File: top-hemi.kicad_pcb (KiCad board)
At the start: 2 copper layers, 46 x 39 mm, 38 parts, among them J1 USB_B_Mini, J2 TC2030_NL, J3 FFC-0.5MM-6POS, J4 Conn_01x02, J5 Conn_01x02, J6 FFC-0.5MM-6POS, J7 Conn_01x02, J8 Conn_01x02, U1 PMIC-LDO-XC6204B332MR_SOT23-5_, U2 LP2985-5.0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

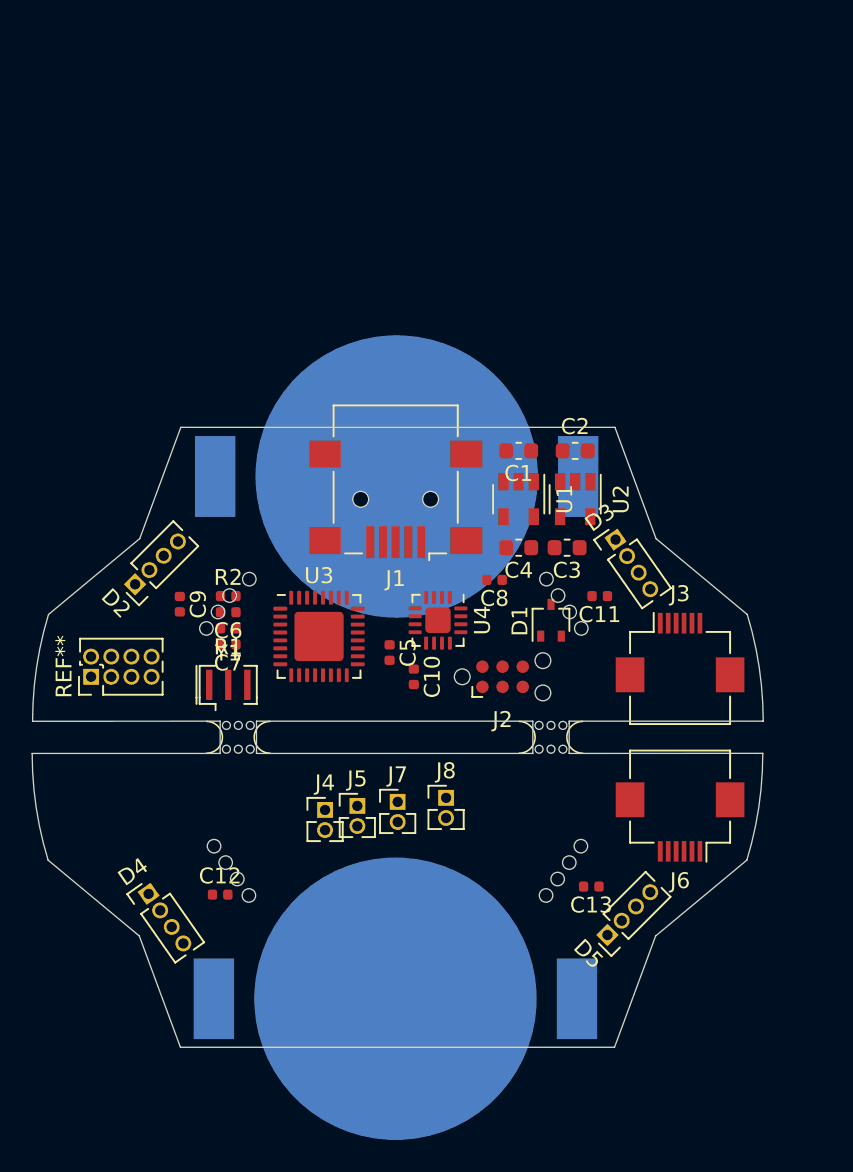
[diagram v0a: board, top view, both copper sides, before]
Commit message: Move BNC connectors to correct hemispheres
Positions within the hemisphere don’t matter.
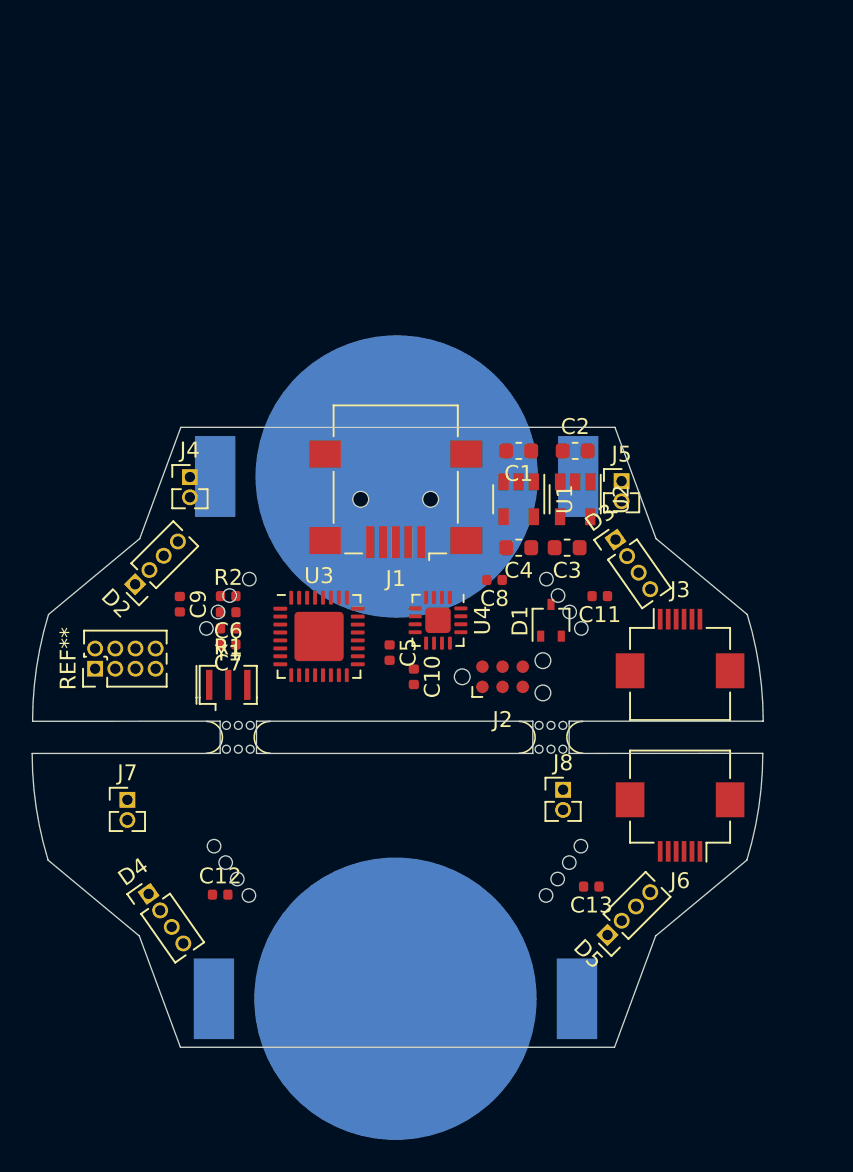
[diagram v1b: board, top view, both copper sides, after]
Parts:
- J4: value Conn_01x02 -> Port_1
- J5: value Conn_01x02 -> Port_2
- J7: value Conn_01x02 -> Port_3
- J8: value Conn_01x02 -> Port_4
- moved J5 26.4 mm to (147.2, 72.5)
- moved J4 22.6 mm to (120.0, 72.3)
- moved J7 17.0 mm to (116.1, 92.6)
- moved J8 7.38 mm to (143.5, 91.9)
- moved REF** 0.57 mm to (114.0, 84.3)
- moved J3 0.25 mm to (150.9, 83.1)
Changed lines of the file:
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@@
   (general
     (thickness 1.6)
-    (drawings 116)
+    (drawings 117)
     (tracks 0)
     (zones 0)
@@
     (0 F.Cu signal)
     (31 B.Cu signal hide)
-    (32 B.Adhes user)
-    (33 F.Adhes user)
-    (34 B.Paste user)
+    (32 B.Adhes user hide)
+    (33 F.Adhes user hide)
+    (34 B.Paste user hide)
     (35 F.Paste user)
-    (36 B.SilkS user)
-    (37 F.SilkS user)
+    (36 B.SilkS user hide)
+    (37 F.SilkS user hide)
     (38 B.Mask user hide)
-    (39 F.Mask user hide)
-    (40 Dwgs.User user hide)
+    (39 F.Mask user)
+    (40 Dwgs.User user)
     (41 Cmts.User user hide)
     (42 Eco1.User user hide)
     (43 Eco2.User user hide)
     (44 Edge.Cuts user)
-    (45 Margin user)
+    (45 Margin user hide)
     (46 B.CrtYd user hide)
-    (47 F.CrtYd user hide)
+    (47 F.CrtYd user)
     (48 B.Fab user hide)
-    (49 F.Fab user hide)
+    (49 F.Fab user)
   )
   (setup
@@
   )
   (module Connector_PinHeader_1.27mm:PinHeader_2x04_P1.27mm_Vertical (layer F.Cu)
-    (at 113.792 84.836 90)
+    (at 114.046 84.328 90)
     (descr "Through hole straight pin header, 2x04, 1.27mm pitch, double rows")
     (tags "Through hole pin header THT 2x04 1.27mm double row")
@@
       (effects (font (size 1 1) (thickness 0.15)))
     )
-    (fp_text user %R (at 0.635 1.905 180) (layer F.Fab)
+    (fp_text user %R (at -2.413 0.762 180) (layer F.Fab)
       (effects (font (size 1 1) (thickness 0.15)))
     )
@@
   )
   (module Connector_FFC-FPC:Hirose_FH12-6S-0.5SH_1x06-1MP_P0.50mm_Horizontal (layer F.Cu)
-    (at 150.876 83.312)
+    (at 150.876 83.058)
     (descr "Molex FH12, FFC/FPC connector, FH12-6S-0.5SH, 6 Pins per row (https://www.hirose.com/product/en/products/FH12/FH12-24S-0.5SH(55)/), generated with kicad-footprint-generator")
     (tags "connector Hirose  top entry")
@@
     (fp_line (start 1.55 4.95) (end 1.55 -1.15) (layer F.CrtYd) (width 0.05))
     (fp_line (start 1.55 -1.15) (end -1.55 -1.15) (layer F.CrtYd) (width 0.05))
-    (fp_text user %R (at 0 1.905 225) (layer F.Fab)
+    (fp_text user %R (at 0.987828 5.862694 225) (layer F.Fab)
       (effects (font (size 1 1) (thickness 0.15)))
     )
@@
   )
   (module Connector_PinHeader_1.27mm:PinHeader_1x02_P1.27mm_Vertical (layer F.Cu)
-    (at 128.524 93.218)
+    (at 120.015 72.263)
     (descr "Through hole straight pin header, 1x02, 1.27mm pitch, single row")
     (tags "Through hole pin header THT 1x02 1.27mm single row")
@@
       (effects (font (size 1 1) (thickness 0.15)))
     )
-    (fp_text value Conn_01x02 (at 0 2.965) (layer F.Fab)
+    (fp_text value Port_1 (at 0 2.965) (layer F.Fab)
       (effects (font (size 1 1) (thickness 0.15)))
     )
@@
   )
   (module Connector_PinHeader_1.27mm:PinHeader_1x02_P1.27mm_Vertical (layer F.Cu)
-    (at 130.556 92.964)
+    (at 147.193 72.517)
     (descr "Through hole straight pin header, 1x02, 1.27mm pitch, single row")
     (tags "Through hole pin header THT 1x02 1.27mm single row")
@@
       (effects (font (size 1 1) (thickness 0.15)))
     )
-    (fp_text value Conn_01x02 (at 0 2.965) (layer F.Fab)
+    (fp_text value Port_2 (at 0 2.965) (layer F.Fab)
       (effects (font (size 1 1) (thickness 0.15)))
     )
@@
   )
   (module Connector_PinHeader_1.27mm:PinHeader_1x02_P1.27mm_Vertical (layer F.Cu)
-    (at 133.096 92.71)
+    (at 116.078 92.583)
     (descr "Through hole straight pin header, 1x02, 1.27mm pitch, single row")
     (tags "Through hole pin header THT 1x02 1.27mm single row")
@@
       (effects (font (size 1 1) (thickness 0.15)))
     )
-    (fp_text value Conn_01x02 (at 0 2.965) (layer F.Fab)
+    (fp_text value Port_3 (at 0 2.965) (layer F.Fab)
       (effects (font (size 1 1) (thickness 0.15)))
     )
@@
   )
   (module Connector_PinHeader_1.27mm:PinHeader_1x02_P1.27mm_Vertical (layer F.Cu)
-    (at 136.144 92.456)
+    (at 143.51 91.948)
     (descr "Through hole straight pin header, 1x02, 1.27mm pitch, single row")
     (tags "Through hole pin header THT 1x02 1.27mm single row")
@@
       (effects (font (size 1 1) (thickness 0.15)))
     )
-    (fp_text value Conn_01x02 (at 0 2.965) (layer F.Fab)
+    (fp_text value Port_4 (at 0 2.965) (layer F.Fab)
       (effects (font (size 1 1) (thickness 0.15)))
     )
@@
       (net 4 "/Bottom hemisphere/BATT-BOT") (die_length 0.20066))
   )
+  (gr_circle (center 152.019 76.708) (end 152.319 76.708) (layer Dwgs.User) (width 0.01))
   (gr_line (start 143.891 87.63) (end 143.891 87.757) (layer Edge.Cuts) (width 0.05))
   (gr_line (start 156.109 87.63) (end 143.891 87.63) (layer Edge.Cuts) (width 0.05))

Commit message: Update contours
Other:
- board size 46 x 39 mm -> 49.7 x 63.9 mm

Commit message: Update panelization
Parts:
- moved mouse-bite-2mm-slot 2.03 mm to (125.1, 88.6)
- moved mouse-bite-2mm-slot 1.64 mm to (141.1, 88.6)
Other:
- board size 49.7 x 63.9 mm -> 46 x 39 mm
- board text removed: "Holder w/ battery (Bottom)"
- board text removed: "LED"
- board text removed: "Micr. USB (Top)"
- board text removed: "Rail / Fixture"

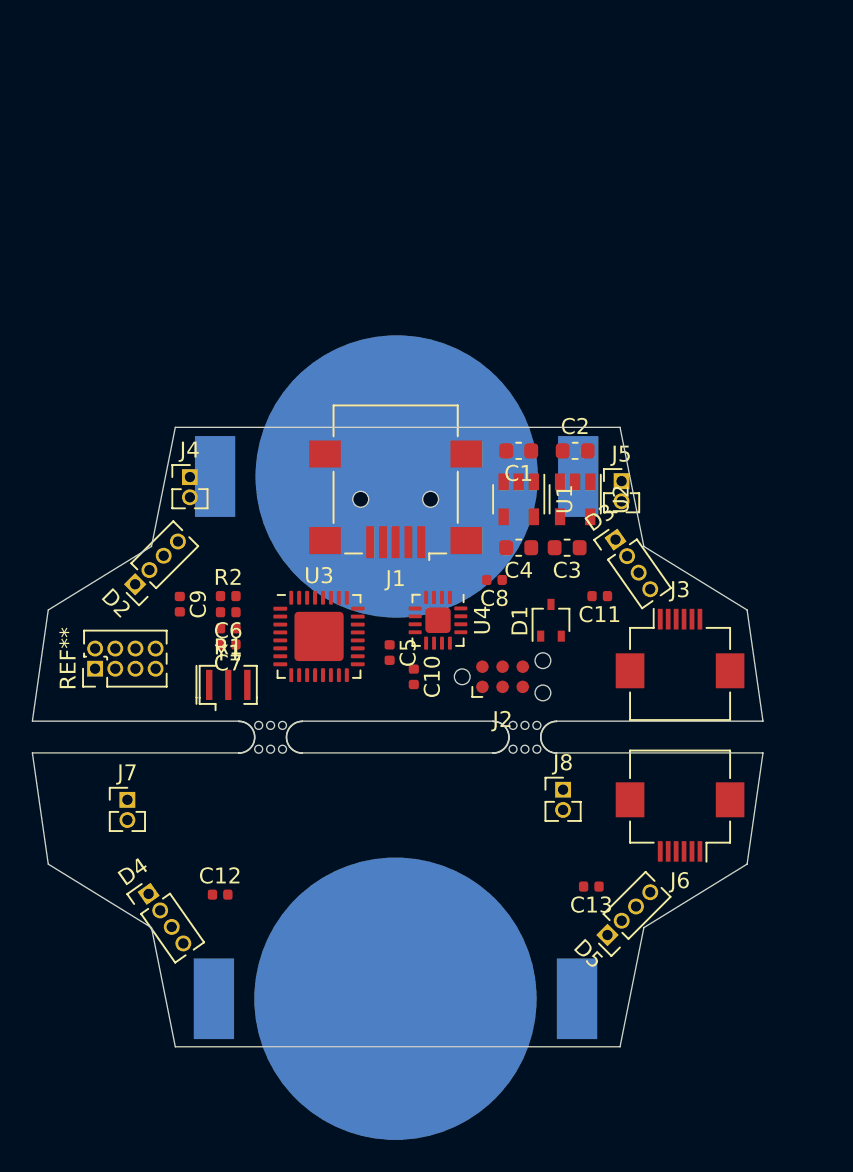
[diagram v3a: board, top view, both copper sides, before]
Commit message: Added initial tracks
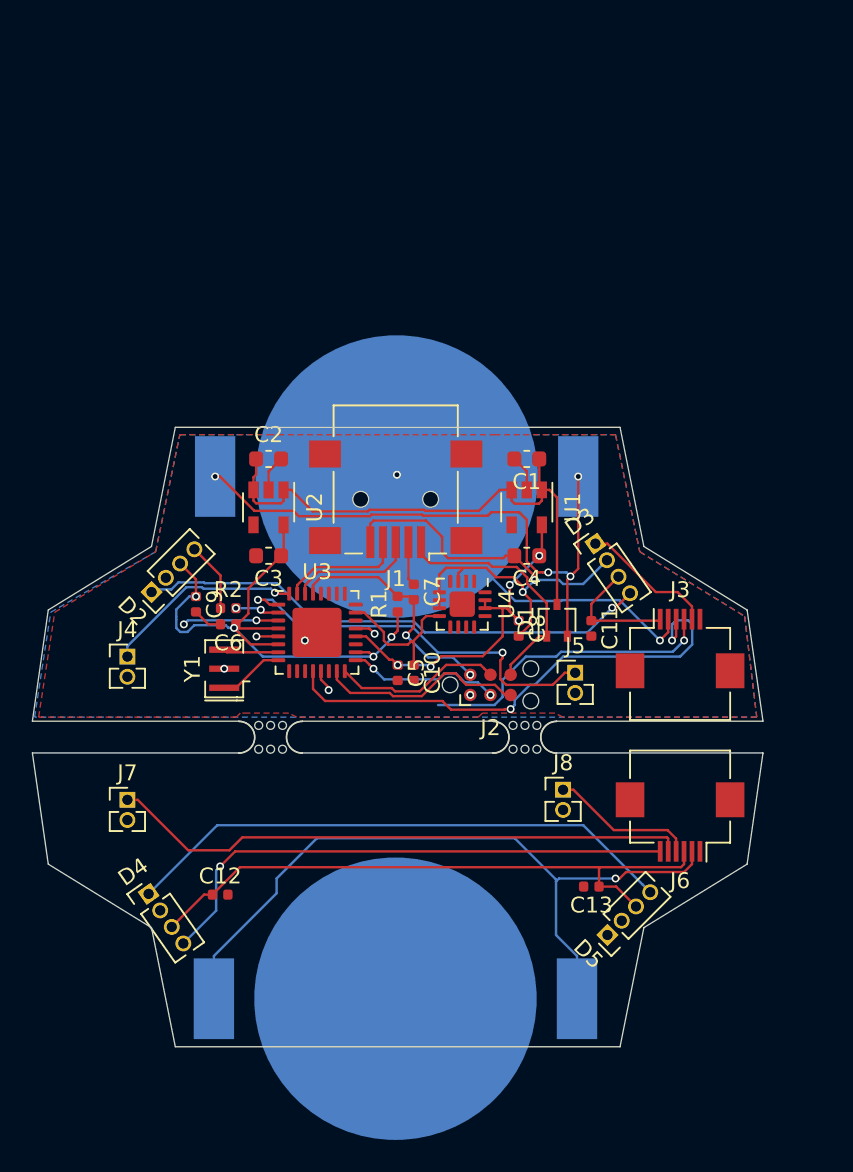
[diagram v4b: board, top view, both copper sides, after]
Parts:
- removed REF**: PinHeader_2x04_P1.27mm_Vertical, Connector_PinHeader_1.27mm:PinHeader_2x04_P1.27mm_Vertical
- moved C2 19.3 mm to (125.0, 71.1)
- moved U2 19.3 mm to (125.0, 74.2)
- moved C3 18.8 mm to (125.0, 77.2)
- moved J5 12.4 mm to (144.3, 84.6)
- moved C7 12.1 mm to (134.1, 79.5), turned to 270 degrees
- moved J4 12.0 mm to (116.1, 83.6)
- moved R1 10.8 mm to (133.1, 80.3), turned to 90 degrees
- moved C8 3.41 mm to (140.7, 81.8), turned to 270 degrees
- moved C11 2.10 mm to (145.3, 81.8), turned to 270 degrees
- moved U4 1.83 mm to (137.2, 80.3)
- moved C5 1.37 mm to (133.1, 84.6)
- moved D3 1.30 mm to (145.5, 76.5)
- moved D2 1.14 mm to (117.6, 79.5)
- moved Y1 1.05 mm to (122.2, 84.3), turned to 90 degrees
- moved C9 1.02 mm to (120.4, 80.3)
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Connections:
- J1 pad 2: /Top Hemisphere/RXI -> /Top Hemisphere/DTR
- J1 pad 3: /Top Hemisphere/DTR -> /Top Hemisphere/RXI
- J1 pad 6: GND -> Net-(J1-Pad6)
- J2 pad 1: /Top Hemisphere/+5V_EXT -> GND
- J2 pad 2: /Top Hemisphere/MOSI -> /Top Hemisphere/~RST
- J2 pad 3: /Top Hemisphere/MISO -> /Top Hemisphere/SCK
- J2 pad 4: /Top Hemisphere/SCK -> /Top Hemisphere/MISO
- J2 pad 5: /Top Hemisphere/~RST -> /Top Hemisphere/MOSI
- J2 pad 6: GND -> /Top Hemisphere/+5V_EXT
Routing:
- net +5V: track 0.00 -> 84.2 mm, vias 0 -> 4
- net GND: track 0.00 -> 48.2 mm, vias 0 -> 9
- net /Bottom hemisphere/BATT-BOT: track 0.00 -> 46.8 mm, vias 0 -> 1
- net /Top Hemisphere/BATT: track 0.00 -> 37.1 mm, vias 0 -> 4
- net /Bottom hemisphere/BNC-3: track 0.00 -> 36.5 mm
- net Net-(D4-Pad1): track 0.00 -> 35.1 mm
- net /Top Hemisphere/VIN: track 0.00 -> 34.3 mm
- net /Bottom hemisphere/DIN-BOT: track 0.00 -> 33.9 mm, vias 0 -> 1
- net Net-(D2-Pad1): track 0.00 -> 33.3 mm, vias 0 -> 1
- net /Top Hemisphere/BNC-3: track 0.00 -> 32.6 mm, vias 0 -> 2
- net /Top Hemisphere/BATT-BOT: track 0.00 -> 28.8 mm, vias 0 -> 2
- net /Top Hemisphere/BNC-2: track 0.00 -> 25.1 mm, vias 0 -> 2
- net +3V3: track 0.00 -> 22.2 mm, vias 0 -> 5
- net /Top Hemisphere/BNC-4: track 0.00 -> 20.5 mm, vias 0 -> 2
- net /Top Hemisphere/+5V_EXT: track 0.00 -> 15.9 mm
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- added copper zone on B.Cu, net GND
- added copper zone on F.Cu, net GND
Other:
- net class Default: clearance 0.2 -> 0.1524; trace_width 0.25 -> 0.1524; via_dia 0.8 -> 0.5; via_drill 0.4 -> 0.3
- rule trace_clearance: 0.2 -> 0.1524
- rule trace_min: 0.2 -> 0.1016
- rule via_min_size: 0.4 -> 0.5

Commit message: Finalised routes
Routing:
- net GND: track 48.2 -> 72.8 mm, vias 9 -> 19
- net +5V: track 84.2 -> 98.9 mm, vias 4 -> 5
- net /Top Hemisphere/BNC-4: track 20.5 -> 28.0 mm
- net Net-(D4-Pad1): track 35.1 -> 37.7 mm
- net /Top Hemisphere/BATT: track 37.1 -> 38.8 mm
- net /Top Hemisphere/MISO: track 10.6 -> 11.7 mm
- net /Top Hemisphere/~RST: track 15.2 -> 16.0 mm
- net +3V3: track 22.2 -> 21.5 mm

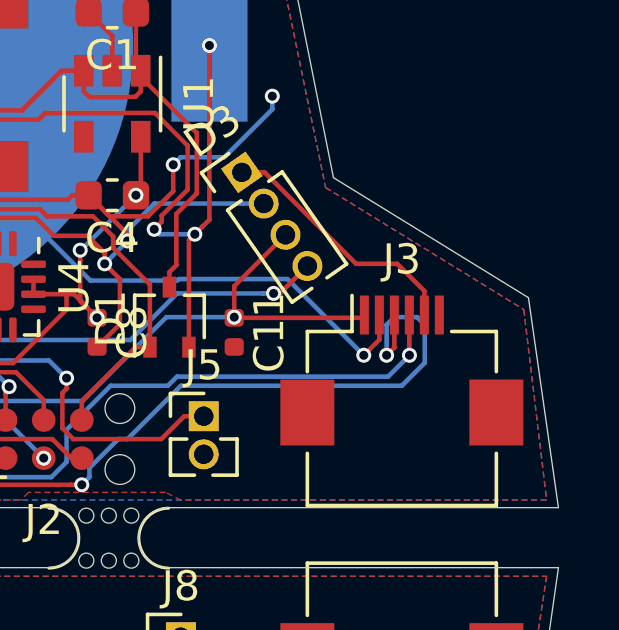
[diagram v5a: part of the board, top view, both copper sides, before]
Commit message: Corrected route not connected
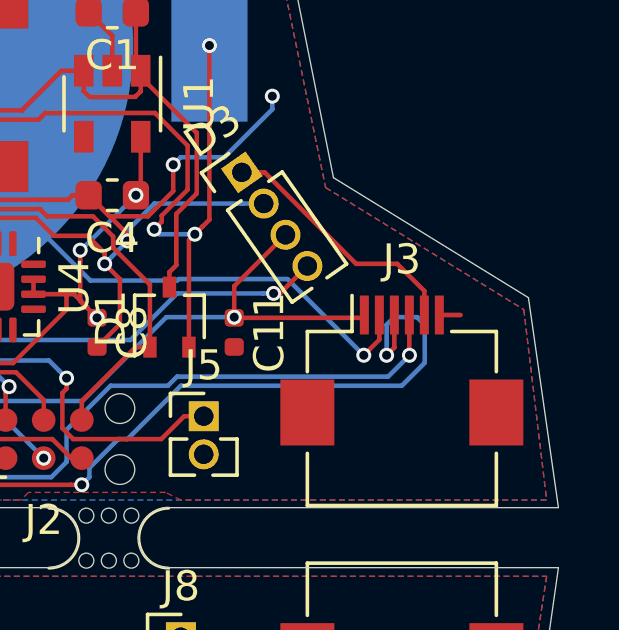
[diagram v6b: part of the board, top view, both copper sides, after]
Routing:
- net GND: track 72.8 -> 73.5 mm
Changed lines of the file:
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@@
     (thickness 1.6)
     (drawings 88)
-    (tracks 492)
+    (tracks 493)
     (zones 0)
     (modules 37)
@@
   (page A4)
   (layers
-    (0 F.Cu signal)
-    (31 B.Cu signal)
+    (0 F.Cu signal hide)
+    (31 B.Cu signal hide)
     (32 B.Adhes user hide)
     (33 F.Adhes user hide)
@@
     (35 F.Paste user)
     (36 B.SilkS user hide)
-    (37 F.SilkS user)
+    (37 F.SilkS user hide)
     (38 B.Mask user hide)
-    (39 F.Mask user)
+    (39 F.Mask user hide)
     (40 Dwgs.User user hide)
     (41 Cmts.User user hide)
@@
     (45 Margin user hide)
     (46 B.CrtYd user hide)
-    (47 F.CrtYd user)
+    (47 F.CrtYd user hide)
     (48 B.Fab user hide)
-    (49 F.Fab user)
+    (49 F.Fab user hide)
   )
   (setup
@@
   (segment (start 152.198 95.758) (end 152.126 95.83) (width 0.1524) (layer F.Cu) (net 3))
   (segment (start 153.416 95.758) (end 152.198 95.758) (width 0.1524) (layer F.Cu) (net 3))
+  (segment (start 152.126 81.208) (end 152.836 81.208) (width 0.1524) (layer F.Cu) (net 3))
   (segment (start 144.3863 102.4128) (end 144.3863 105.1052) (width 0.1524) (layer B.Cu) (net 4))
   (segment (start 143.0655 101.092) (end 144.3863 102.4128) (width 0.1524) (layer B.Cu) (net 4))

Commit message: Updated PCB
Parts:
- moved C9 0.38 mm to (120.7, 80.5)
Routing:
- net /Top Hemisphere/BATT-BOT: vias 2 -> 1
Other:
- rule via_min_size: 0.5 -> 0.3
- board text added: "DIN"
- board text added: "GND"
